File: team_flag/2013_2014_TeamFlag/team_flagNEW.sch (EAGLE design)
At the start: 7 parts, among them Q1 MOSFET-NCHANNELSMD, Q2 MOSFET-NCHANNELSMD

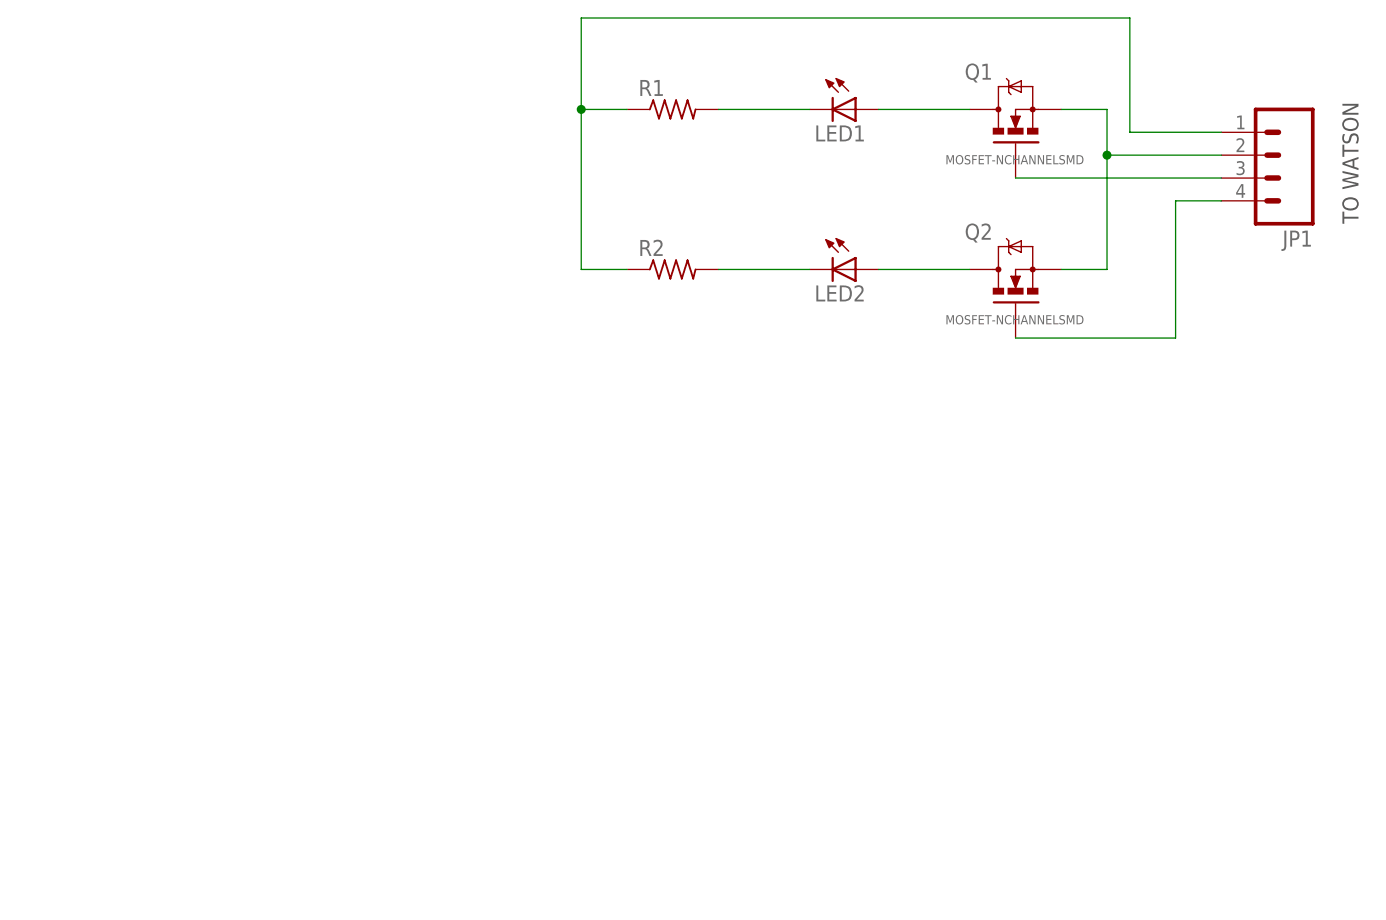
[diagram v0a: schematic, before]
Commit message: Team Flag - Rev A
-Rewired MOSFETs correctly
-Repositioned bottom silkscreen text and updated information
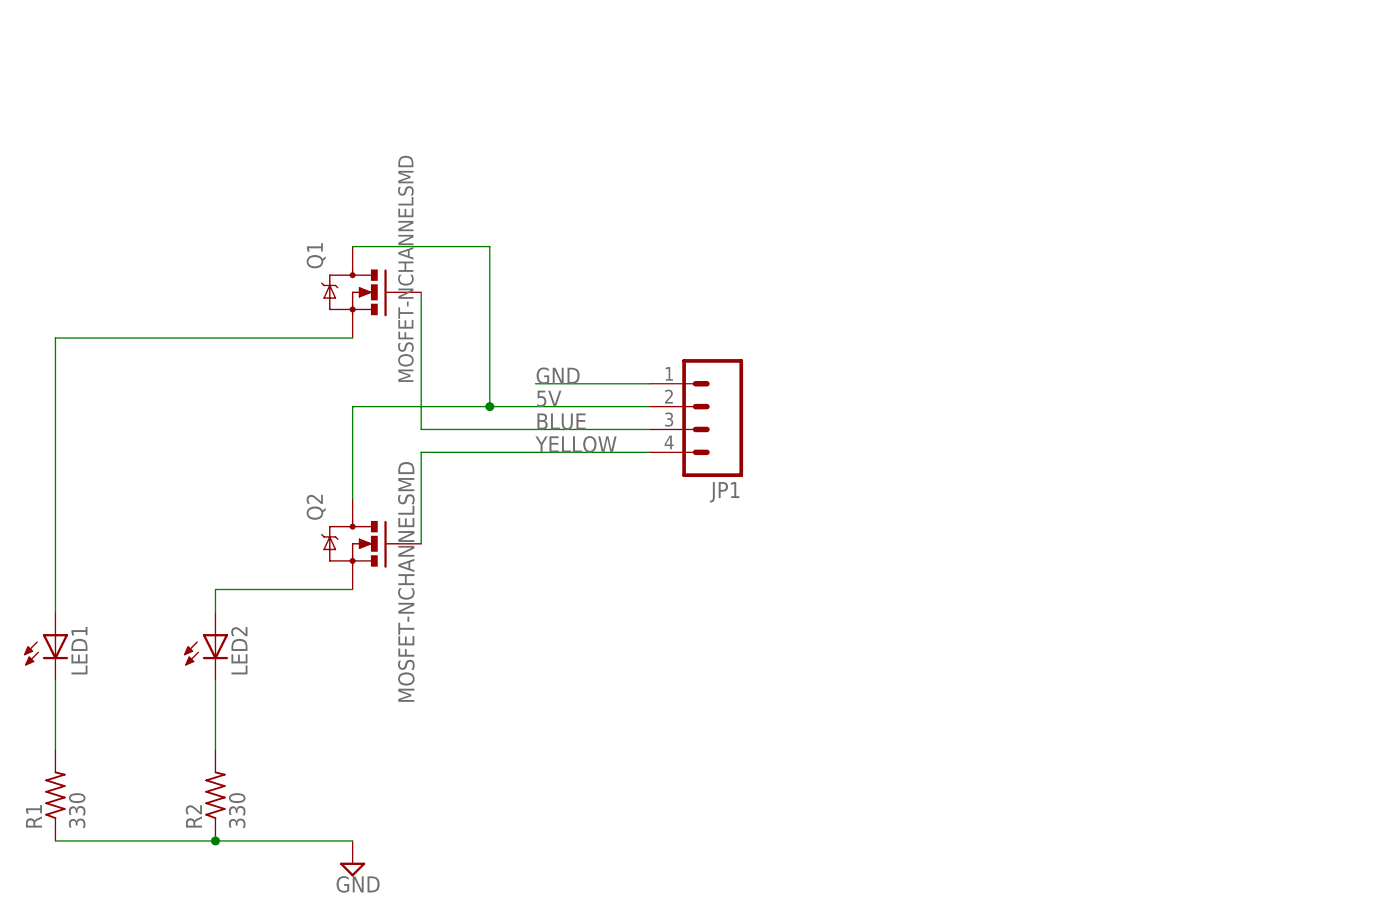
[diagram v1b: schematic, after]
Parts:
- R1, R2: value (none) -> 330
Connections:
- net 5V: now also Q1.D, Q2.D; no longer Q1.S, Q2.S
- net BDRAIN: now also LED1.C, R1.2; no longer LED2.C, R2.2
- net BLUE: now also JP1.3, Q1.G; no longer JP1.4, Q2.G
- net BSIGNAL: now also LED1.A, Q1.S; no longer LED2.A, Q2.D
- net YDRAIN: now also LED2.C, R2.2; no longer LED1.C, R1.2
- net YELLOW: now also JP1.4, Q2.G; no longer JP1.3, Q1.G
- net YSIGNAL: now also LED2.A, Q2.S; no longer LED1.A, Q1.D
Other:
- note removed: "TO WATSON"
- moved on the sheet: JP1, LED1, LED2, Q1, Q2, R1, R2
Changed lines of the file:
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@@
 <part name="LED1" library="led" deviceset="LED" device="5MM"/>
 <part name="LED2" library="led" deviceset="LED" device="5MM"/>
-<part name="R1" library="rcl" deviceset="R-US_" device="R0603"/>
-<part name="R2" library="rcl" deviceset="R-US_" device="R0603"/>
+<part name="R1" library="rcl" deviceset="R-US_" device="R0603" value="330"/>
+<part name="R2" library="rcl" deviceset="R-US_" device="R0603" value="330"/>
 <part name="Q1" library="pie" deviceset="MOSFET-NCHANNEL" device="SMD"/>
 <part name="Q2" library="pie" deviceset="MOSFET-NCHANNEL" device="SMD"/>
 <part name="JP1" library="pie" deviceset="M04" device="PTH"/>
+<part name="SUPPLY1" library="pie" deviceset="GND" device=""/>
 </parts>
 <sheets>
 <sheet>
 <plain>
-<text x="91.44" y="45.72" size="1.778" layer="97" font="vector" rot="R90">TO WATSON</text>
 </plain>
 <instances>
-<instance part="LED1" gate="G$1" x="35.56" y="58.42" rot="R270"/>
-<instance part="LED2" gate="G$1" x="35.56" y="40.64" rot="R270"/>
-<instance part="R1" gate="G$1" x="15.24" y="58.42"/>
-<instance part="R2" gate="G$1" x="15.24" y="40.64"/>
-<instance part="Q1" gate="G$1" x="53.34" y="58.42" smashed="yes" rot="R90">
-<attribute name="NAME" x="50.8" y="63.5" size="1.778" layer="95" rot="R180"/>
-<attribute name="VALUE" x="60.96" y="53.34" size="1.016" layer="96" rot="R180"/>
+<instance part="LED1" gate="G$1" x="-53.34" y="0"/>
+<instance part="LED2" gate="G$1" x="-35.56" y="0"/>
+<instance part="R1" gate="G$1" x="-53.34" y="-17.78" rot="R90"/>
+<instance part="R2" gate="G$1" x="-35.56" y="-17.78" rot="R90"/>
+<instance part="Q1" gate="G$1" x="-20.32" y="38.1" smashed="yes" rot="MR0">
+<attribute name="NAME" x="-25.4" y="40.64" size="1.778" layer="95" rot="MR90"/>
+<attribute name="VALUE" x="-15.24" y="27.94" size="1.6764" layer="96" rot="MR90"/>
 </instance>
-<instance part="Q2" gate="G$1" x="53.34" y="40.64" smashed="yes" rot="R90">
-<attribute name="NAME" x="50.8" y="45.72" size="1.778" layer="95" rot="R180"/>
-<attribute name="VALUE" x="60.96" y="35.56" size="1.016" layer="96" rot="R180"/>
+<instance part="Q2" gate="G$1" x="-20.32" y="10.16" smashed="yes" rot="MR0">
+<attribute name="NAME" x="-25.4" y="12.7" size="1.778" layer="95" rot="MR90"/>
+<attribute name="VALUE" x="-15.24" y="-7.62" size="1.778" layer="96" rot="MR90"/>
 </instance>
-<instance part="JP1" gate="G$1" x="83.82" y="53.34" rot="R180"/>
+<instance part="JP1" gate="G$1" x="20.32" y="25.4" rot="R180"/>
+<instance part="SUPPLY1" gate="GND" x="-20.32" y="-25.4"/>
 </instances>
 <busses>
 </busses>
 <nets>
+<net name="YELLOW" class="0">
+<segment>
+<pinref part="JP1" gate="G$1" pin="4"/>
+<wire x1="12.7" y1="20.32" x2="-12.7" y2="20.32" width="0.1524" layer="91"/>
+<wire x1="-12.7" y1="20.32" x2="-12.7" y2="10.16" width="0.1524" layer="91"/>
+<pinref part="Q2" gate="G$1" pin="G"/>
+<label x="0" y="20.32" size="1.778" layer="95"/>
+</segment>
+</net>
+<net name="BLUE" class="0">
+<segment>
+<pinref part="JP1" gate="G$1" pin="3"/>
+<wire x1="12.7" y1="22.86" x2="-12.7" y2="22.86" width="0.1524" layer="91"/>
+<wire x1="-12.7" y1="22.86" x2="-12.7" y2="38.1" width="0.1524" layer="91"/>
+<pinref part="Q1" gate="G$1" pin="G"/>
+<label x="0" y="22.86" size="1.778" layer="95"/>
+</segment>
+</net>
 <net name="5V" class="0">
 <segment>
 <pinref part="JP1" gate="G$1" pin="2"/>
-<wire x1="76.2" y1="53.34" x2="63.5" y2="53.34" width="0.1524" layer="91"/>
-<wire x1="63.5" y1="53.34" x2="63.5" y2="58.42" width="0.1524" layer="91"/>
-<pinref part="Q1" gate="G$1" pin="S"/>
-<wire x1="63.5" y1="58.42" x2="58.42" y2="58.42" width="0.1524" layer="91"/>
-<pinref part="Q2" gate="G$1" pin="S"/>
-<wire x1="63.5" y1="53.34" x2="63.5" y2="40.64" width="0.1524" layer="91"/>
-<wire x1="63.5" y1="40.64" x2="58.42" y2="40.64" width="0.1524" layer="91"/>
-<junction x="63.5" y="53.34"/>
+<wire x1="12.7" y1="25.4" x2="-5.08" y2="25.4" width="0.1524" layer="91"/>
+<pinref part="Q1" gate="G$1" pin="D"/>
+<wire x1="-5.08" y1="25.4" x2="-5.08" y2="43.18" width="0.1524" layer="91"/>
+<wire x1="-5.08" y1="43.18" x2="-20.32" y2="43.18" width="0.1524" layer="91"/>
+<pinref part="Q2" gate="G$1" pin="D"/>
+<wire x1="-5.08" y1="25.4" x2="-20.32" y2="25.4" width="0.1524" layer="91"/>
+<wire x1="-20.32" y1="25.4" x2="-20.32" y2="15.24" width="0.1524" layer="91"/>
+<junction x="-5.08" y="25.4"/>
+<label x="0" y="25.4" size="1.778" layer="95"/>
 </segment>
 </net>
 <net name="YSIGNAL" class="0">
 <segment>
-<pinref part="Q1" gate="G$1" pin="D"/>
-<pinref part="LED1" gate="G$1" pin="A"/>
-<wire x1="48.26" y1="58.42" x2="38.1" y2="58.42" width="0.1524" layer="91"/>
+<pinref part="Q2" gate="G$1" pin="S"/>
+<wire x1="-20.32" y1="5.08" x2="-35.56" y2="5.08" width="0.1524" layer="91"/>
+<pinref part="LED2" gate="G$1" pin="A"/>
+<wire x1="-35.56" y1="5.08" x2="-35.56" y2="2.54" width="0.1524" layer="91"/>
 </segment>
 </net>
 <net name="BSIGNAL" class="0">
 <segment>
-<pinref part="Q2" gate="G$1" pin="D"/>
-<pinref part="LED2" gate="G$1" pin="A"/>
-<wire x1="48.26" y1="40.64" x2="38.1" y2="40.64" width="0.1524" layer="91"/>
+<pinref part="LED1" gate="G$1" pin="A"/>
+<pinref part="Q1" gate="G$1" pin="S"/>
+<wire x1="-53.34" y1="2.54" x2="-53.34" y2="33.02" width="0.1524" layer="91"/>
+<wire x1="-53.34" y1="33.02" x2="-20.32" y2="33.02" width="0.1524" layer="91"/>
+</segment>
+</net>
+<net name="BDRAIN" class="0">
+<segment>
+<pinref part="LED1" gate="G$1" pin="C"/>
+<pinref part="R1" gate="G$1" pin="2"/>
+<wire x1="-53.34" y1="-5.08" x2="-53.34" y2="-12.7" width="0.1524" layer="91"/>
 </segment>
 </net>
 <net name="YDRAIN" class="0">
 <segment>
-<pinref part="LED1" gate="G$1" pin="C"/>
-<pinref part="R1" gate="G$1" pin="2"/>
-<wire x1="30.48" y1="58.42" x2="20.32" y2="58.42" width="0.1524" layer="91"/>
-</segment>
-</net>
-<net name="BDRAIN" class="0">
-<segment>
 <pinref part="LED2" gate="G$1" pin="C"/>
 <pinref part="R2" gate="G$1" pin="2"/>
-<wire x1="30.48" y1="40.64" x2="20.32" y2="40.64" width="0.1524" layer="91"/>
+<wire x1="-35.56" y1="-5.08" x2="-35.56" y2="-12.7" width="0.1524" layer="91"/>
 </segment>
 </net>
 <net name="GND" class="0">
 <segment>
+<pinref part="R1" gate="G$1" pin="1"/>
 <pinref part="R2" gate="G$1" pin="1"/>
-<wire x1="10.16" y1="40.64" x2="5.08" y2="40.64" width="0.1524" layer="91"/>
-<wire x1="5.08" y1="40.64" x2="5.08" y2="58.42" width="0.1524" layer="91"/>
-<pinref part="R1" gate="G$1" pin="1"/>
-<wire x1="5.08" y1="58.42" x2="10.16" y2="58.42" width="0.1524" layer="91"/>
-<wire x1="5.08" y1="58.42" x2="5.08" y2="68.58" width="0.1524" layer="91"/>
-<wire x1="5.08" y1="68.58" x2="66.04" y2="68.58" width="0.1524" layer="91"/>
+<wire x1="-53.34" y1="-22.86" x2="-35.56" y2="-22.86" width="0.1524" layer="91"/>
+<wire x1="-35.56" y1="-22.86" x2="-20.32" y2="-22.86" width="0.1524" layer="91"/>
+<pinref part="SUPPLY1" gate="GND" pin="GND"/>
+<junction x="-35.56" y="-22.86"/>
+</segment>
+<segment>
 <pinref part="JP1" gate="G$1" pin="1"/>
-<wire x1="66.04" y1="68.58" x2="66.04" y2="55.88" width="0.1524" layer="91"/>
-<wire x1="66.04" y1="55.88" x2="76.2" y2="55.88" width="0.1524" layer="91"/>
-<junction x="5.08" y="58.42"/>
+<wire x1="12.7" y1="27.94" x2="0" y2="27.94" width="0.1524" layer="91"/>
+<label x="0" y="27.94" size="1.778" layer="95"/>
 </segment>
 </net>
-<net name="YELLOW" class="0">
-<segment>
-<pinref part="JP1" gate="G$1" pin="3"/>
-<pinref part="Q1" gate="G$1" pin="G"/>
-<wire x1="76.2" y1="50.8" x2="53.34" y2="50.8" width="0.1524" layer="91"/>
-</segment>
-</net>
-<net name="BLUE" class="0">
-<segment>
-<pinref part="JP1" gate="G$1" pin="4"/>
-<wire x1="76.2" y1="48.26" x2="71.12" y2="48.26" width="0.1524" layer="91"/>
-<wire x1="71.12" y1="48.26" x2="71.12" y2="33.02" width="0.1524" layer="91"/>
-<pinref part="Q2" gate="G$1" pin="G"/>
-<wire x1="71.12" y1="33.02" x2="53.34" y2="33.02" width="0.1524" layer="91"/>
-</segment>
-</net>
